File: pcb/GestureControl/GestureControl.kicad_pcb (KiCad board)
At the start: 4 copper layers, 95.3 x 95.3 mm, 179 parts, among them J1 Conn_01x04_I2I-LCD, J10 EXTERN I2C, J11 Conn_01x02, J12 Conn_01x02, J17 Conn_01x01, J18 Conn_01x01, J19 Conn_01x01, J2 BATT, J3 Conn_01x08, J4 Conn_01x06, J5 Conn_01x10, J6 Conn_01x08, J7 FTDI, J8 Conn_01x06, J9 UART, SW1 SW1, SW2 SW2, U1 AP5100_3.3, U10 VL53L3CXV0DH_RIGHT, U11 VL53L3CXV0DH_LEFT, U12 VL53L3CXV0DH_CENTER, U13 VL53L3CXV0DH_CENTER, U2 AP5100_3.3, U3 VL53L3CXV0DH_CENTER, U4 VL53L3CXV0DH_RIGHT, U5 VL53L3CXV0DH_LEFT, U6 STM32L151RETx, U7 STM32F401RETx, U8 VL53L3CXV0DH_RIGHT, U9 VL53L3CXV0DH_LEFT, Y1 8MHz, Y2 32kHz

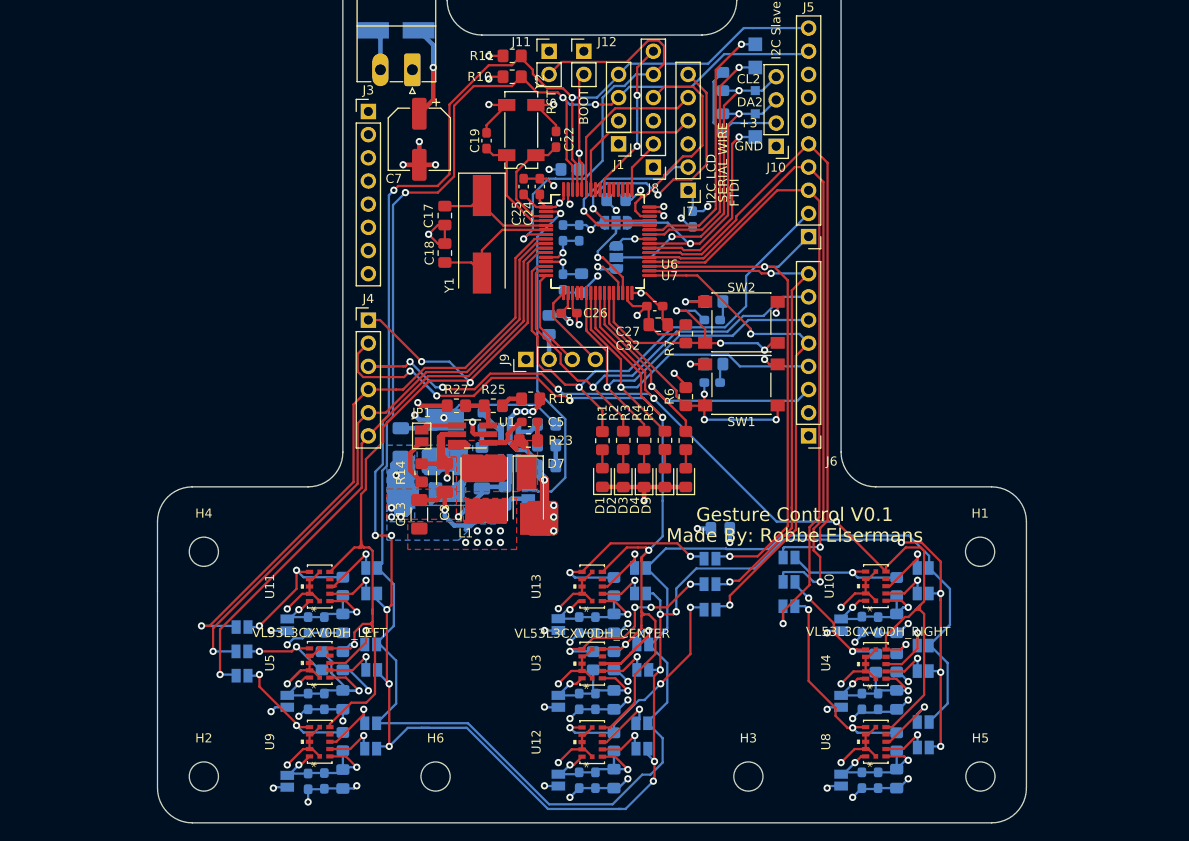
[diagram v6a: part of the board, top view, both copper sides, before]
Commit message: pcb groter maken
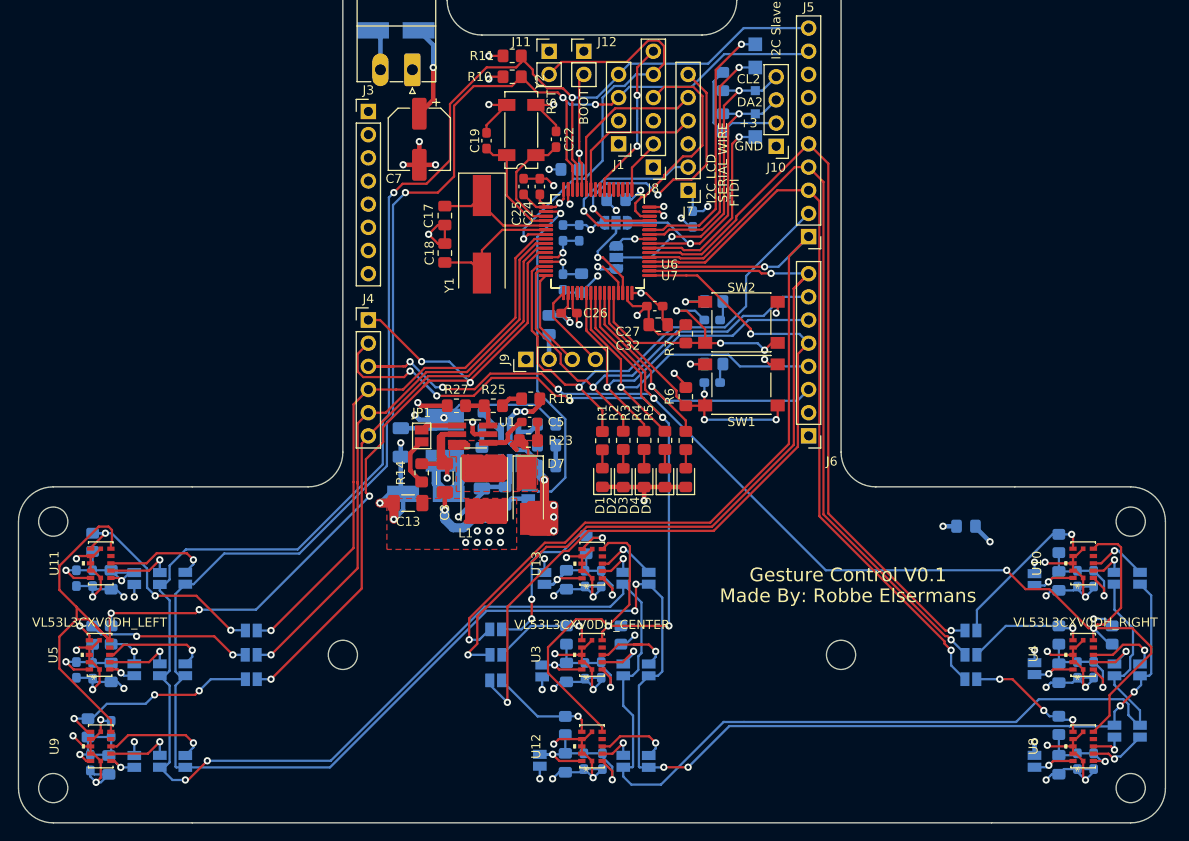
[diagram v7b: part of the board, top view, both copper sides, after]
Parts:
- moved H5 105.4 mm to (87.4, 100.1)
- moved H2 101.6 mm to (205.5, 129.3)
- moved H4 30.7 mm to (87.4, 129.3)
- moved R36 28.0 mm to (91.2, 122.7)
- moved R17 27.9 mm to (91.7, 102.3)
- moved C12 26.9 mm to (187.4, 100.6)
- moved C43 25.9 mm to (89.9, 106.3)
- moved C51 25.9 mm to (91.7, 106.3)
- moved C39 25.9 mm to (201.4, 106.3)
- moved C45 25.8 mm to (93.7, 106.4)
- moved C44 25.7 mm to (91.4, 126.5)
- moved C46 25.7 mm to (93.5, 126.7)
- moved C40 25.6 mm to (201.4, 116.3)
- moved C15 25.6 mm to (89.9, 116.3)
- moved C14 25.6 mm to (91.7, 116.4)
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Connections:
- J3 pad 1: Net-(J3-Pad1) -> (no net)
- J3 pad 2: Net-(J3-Pad2) -> (no net)
- J3 pad 3: Net-(J3-Pad3) -> (no net)
- J3 pad 8: Net-(J3-Pad8) -> (no net)
- J5 pad 6: Net-(J5-Pad6) -> (no net)
- J6 pad 1: Net-(J6-Pad1) -> (no net)
- J6 pad 2: Net-(J6-Pad2) -> (no net)
- U10 pad 8: Net-(U10-Pad8) -> (no net)
- U11 pad 8: Net-(U11-Pad8) -> (no net)
- U12 pad 8: Net-(U12-Pad8) -> (no net)
- U13 pad 8: Net-(U13-Pad8) -> (no net)
- U3 pad 8: Net-(U3-Pad8) -> (no net)
- U4 pad 8: Net-(U4-Pad8) -> (no net)
- U5 pad 8: Net-(U5-Pad8) -> (no net)
- U6 pad 20: Net-(U6-Pad20) -> (no net)
- U6 pad 21: Net-(U6-Pad21) -> (no net)
- U6 pad 50: Net-(U6-Pad50) -> (no net)
- U6 pad 51: Net-(U6-Pad51) -> (no net)
- U6 pad 52: Net-(U6-Pad52) -> (no net)
- U6 pad 53: Net-(U6-Pad53) -> (no net)
- U6 pad 54: Net-(U6-Pad54) -> (no net)
- U6 pad 56: Net-(U6-Pad56) -> (no net)
- U6 pad 57: Net-(U6-Pad57) -> (no net)
- U7 pad 20: Net-(U7-Pad20) -> (no net)
- U7 pad 21: Net-(U7-Pad21) -> (no net)
- U7 pad 50: Net-(U7-Pad50) -> (no net)
- U7 pad 51: Net-(U7-Pad51) -> (no net)
- U7 pad 52: Net-(U7-Pad52) -> (no net)
- U7 pad 53: Net-(U7-Pad53) -> (no net)
- U7 pad 54: Net-(U7-Pad54) -> (no net)
- U7 pad 56: Net-(U7-Pad56) -> (no net)
- U7 pad 57: Net-(U7-Pad57) -> (no net)
- U8 pad 8: Net-(U8-Pad8) -> (no net)
- U9 pad 8: Net-(U9-Pad8) -> (no net)
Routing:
- net SCL1: track 263.4 -> 322.2 mm, vias 16 -> 4
- net SDA1: track 249.7 -> 305.3 mm, vias 3 -> 9
- net GPIOI_0: track 98.2 -> 133.8 mm, vias 3 -> 5
- net _XSHUT_1: track 58.2 -> 90.5 mm
- net +3V3: track 517.2 -> 549.2 mm, vias 35 -> 34
- net _XSHUT_4: track 57.7 -> 89.3 mm
- net _XSHUT_7: track 54.9 -> 85.5 mm
- net /OUT5.0: track 40.4 -> 13.8 mm
- net GPIOI_2: track 124.9 -> 148.4 mm
- net XSHUT_7: track 25.5 -> 11.9 mm, vias 3 -> 1
- net _XSHUT_2: track 73.3 -> 84.5 mm
- net GPIOI_1: track 115.7 -> 126.3 mm
- net XSHUT_3: track 10.9 -> 21.5 mm, vias 2 -> 3
- net XSHUT_0: track 16.0 -> 26.2 mm, vias 2 -> 3
- net XSHUT_4: track 21.6 -> 11.5 mm, vias 4 -> 1
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- removed copper zone on B.Cu, net /OUT5.0
- removed copper zone on B.Cu, net GND
- removed copper zone on F.Cu, net GND
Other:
- board size 95.3 x 95.3 mm -> 125.7 x 95.3 mm

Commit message: add PCB V12
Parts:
- removed C43, C44, C47, C48, C49, C50, C51, C52: 100n, Capacitor_SMD:C_0603_1608Metric_Pad1.08x0.95mm_HandSolder
- removed C45, C46, C53, C54, C55: 4.7µ, Capacitor_SMD:C_0805_2012Metric_Pad1.18x1.45mm_HandSolder
- removed JP10, JP11, JP12, JP14, JP15, JP16, JP17, JP18, JP19, JP20, JP21, JP22, JP23, JP27, JP28, JP29, JP30, JP31, JP32, JP33, JP34, JP35, JP36, JP37, JP38, JP39, JP40, JP41, JP42, JP43, JP44, JP5, JP6, JP7, JP8, JP9: SolderJumper_2_Open, Jumper:SolderJumper-2_P1.3mm_Open_Pad1.0x1.5mm
- removed R33, R34, R35, R36: 10k, Resistor_SMD:R_0805_2012Metric_Pad1.20x1.40mm_HandSolder
- removed U10: VL53L3CXV0DH_RIGHT, VL53L3CX:VL53L3CXV0DH&slash_1
- removed U11, U9: VL53L3CXV0DH_LEFT, VL53L3CX:VL53L3CXV0DH&slash_1
- removed U12, U13: VL53L3CXV0DH_CENTER, VL53L3CX:VL53L3CXV0DH&slash_1
- added C20: 100n, Capacitor_SMD:C_0603_1608Metric_Pad1.08x0.95mm_HandSolder, B.Cu at (201.4, 129.6)
- added C21: 100n, Capacitor_SMD:C_0603_1608Metric_Pad1.08x0.95mm_HandSolder, B.Cu at (239.5, 129.6)
- added H10: MountingHole, MountingHole:MountingHole_3.2mm_M3, F.Cu at (111.5, 108.5)
- added H11: MountingHole, MountingHole:MountingHole_3.2mm_M3, F.Cu at (187.7, 143.4)
- added H12: MountingHole, MountingHole:MountingHole_3.2mm_M3, F.Cu at (187.7, 118.0)
- added H13: MountingHole, MountingHole:MountingHole_3.2mm_M3, F.Cu at (225.8, 118.0)
- added H14: MountingHole, MountingHole:MountingHole_3.2mm_M3, F.Cu at (225.8, 143.4)
- added H15: MountingHole, MountingHole:MountingHole_3.2mm_M3, F.Cu at (251.2, 118.0)
- added H16: MountingHole, MountingHole:MountingHole_3.2mm_M3, F.Cu at (251.2, 143.4)
- added H7: MountingHole, MountingHole:MountingHole_3.2mm_M3, F.Cu at (138.2, 108.5)
- added H8: MountingHole, MountingHole:MountingHole_3.2mm_M3, F.Cu at (111.5, 152.9)
- added H9: MountingHole, MountingHole:MountingHole_3.2mm_M3, F.Cu at (138.2, 152.9)
- added J13: 690367291076, WR-MM Female SMT Connector:WR-MM_Female_SMT_Connector, B.Cu at (162.3, 136.4)
- added J14: 690367291076, WR-MM Female SMT Connector:WR-MM_Female_SMT_Connector, B.Cu at (200.4, 136.4)
- added J15: 690367291076, WR-MM Female SMT Connector:WR-MM_Female_SMT_Connector, B.Cu at (238.5, 136.4)
- added J16: 690367291076, WR-MM Female SMT Connector:WR-MM_Female_SMT_Connector, B.Cu at (124.8, 148.7)
- added J20: 690367291076, WR-MM Female SMT Connector:WR-MM_Female_SMT_Connector, B.Cu at (124.8, 112.6)
- added J21: 690367291076, WR-MM Female SMT Connector:WR-MM_Female_SMT_Connector, B.Cu at (124.8, 137.4)
- added TP10: TestPoint, TestPoint:TestPoint_Pad_D2.0mm, B.Cu at (200.2, 115.6)
- added TP11: TestPoint, TestPoint:TestPoint_Pad_D2.0mm, B.Cu at (197.1, 118.9)
- added TP12: TestPoint, TestPoint:TestPoint_Pad_D2.0mm, B.Cu at (200.2, 118.9)
- added TP13: TestPoint, TestPoint:TestPoint_Pad_D2.0mm, B.Cu at (203.2, 115.6)
- added TP14: TestPoint, TestPoint:TestPoint_Pad_D2.0mm, B.Cu at (203.2, 118.9)
- added TP15: TestPoint, TestPoint:TestPoint_Pad_D2.0mm, B.Cu at (235.2, 115.6)
- added TP16: TestPoint, TestPoint:TestPoint_Pad_D2.0mm, B.Cu at (238.3, 115.6)
- added TP17: TestPoint, TestPoint:TestPoint_Pad_D2.0mm, B.Cu at (235.2, 118.9)
- added TP18: TestPoint, TestPoint:TestPoint_Pad_D2.0mm, B.Cu at (238.3, 118.9)
- added TP19: TestPoint, TestPoint:TestPoint_Pad_D2.0mm, B.Cu at (241.3, 115.6)
- added TP20: TestPoint, TestPoint:TestPoint_Pad_D2.0mm, B.Cu at (241.3, 118.9)
- added TP3: TestPoint, TestPoint:TestPoint_Pad_D2.0mm, B.Cu at (158.9, 115.6)
- added TP4: TestPoint, TestPoint:TestPoint_Pad_D2.0mm, B.Cu at (162.1, 115.6)
- added TP5: TestPoint, TestPoint:TestPoint_Pad_D2.0mm, B.Cu at (158.9, 118.9)
- added TP6: TestPoint, TestPoint:TestPoint_Pad_D2.0mm, B.Cu at (162.1, 118.9)
- added TP7: TestPoint, TestPoint:TestPoint_Pad_D2.0mm, B.Cu at (165.2, 115.6)
- added TP8: TestPoint, TestPoint:TestPoint_Pad_D2.0mm, B.Cu at (165.2, 118.9)
- added TP9: TestPoint, TestPoint:TestPoint_Pad_D2.0mm, B.Cu at (197.1, 115.6)
- C16: value 4.7µ -> 100n; footprint Capacitor_SMD:C_0805_2012Metric_Pad1.18x1.45mm_HandSolder -> Capacitor_SMD:C_0603_1608Metric_Pad1.08x0.95mm_HandSolder
- C36: value 100n -> 4.7µ; footprint Capacitor_SMD:C_0603_1608Metric_Pad1.08x0.95mm_HandSolder -> Capacitor_SMD:C_0805_2012Metric_Pad1.18x1.45mm_HandSolder
- C39, C40, C41, C42: value 100n -> 10µ; footprint Capacitor_SMD:C_0603_1608Metric_Pad1.08x0.95mm_HandSolder -> Capacitor_SMD:C_1206_3216Metric_Pad1.33x1.80mm_HandSolder
- U3: value VL53L3CXV0DH_CENTER -> VL53L3CXV0DH_1
- U4, U8: value VL53L3CXV0DH_RIGHT -> VL53L3CXV0DH_1
- U5: value VL53L3CXV0DH_LEFT -> VL53L3CXV0DH_1
- moved R17 149.7 mm to (235.7, 143.3)
- moved C15 148.4 mm to (237.7, 129.6), turned to 90 degrees
- moved J19 130.3 mm to (51.4, 112.8), turned to 270 degrees
- moved D6 129.8 mm to (49.9, 152.2), turned to 270 degrees
- moved H5 127.0 mm to (213.1, 118.0)
- moved J18 126.8 mm to (54.0, 112.8), turned to 270 degrees
- moved J12 124.9 mm to (52.2, 131.6), turned to 90 degrees
- moved J11 124.8 mm to (52.2, 135.4), turned to 90 degrees
- moved R11 124.1 mm to (52.7, 139.4), turned to 90 degrees
- moved R22 123.5 mm to (55.5, 116.3), turned to 0 degrees
- moved J2 123.4 mm to (54.2, 150.4), turned to 270 degrees
- moved TP2 123.4 mm to (56.5, 112.8), turned to 270 degrees
- moved R10 120.8 mm to (55.0, 139.4), turned to 90 degrees
- moved TP1 119.9 mm to (59.1, 112.8), turned to 270 degrees
- moved J3 118.3 mm to (58.8, 155.2), turned to 90 degrees
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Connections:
- C10 pad 1: /VL53L3CX center/PWR1 -> +3V3
- C14 pad 1: /VL53L3CX left/PWR1 -> +3V3
- C15 pad 1: /VL53L3CX left/PWR1 -> +3V3
- C16 pad 1: /VL53L3CX left/PWR1 -> +3V3
- C35 pad 1: /VL53L3CX center/PWR0 -> +3V3
- C36 pad 1: /VL53L3CX center/PWR2 -> +3V3
- C37 pad 1: /VL53L3CX center/PWR0 -> +3V3
- C38 pad 1: /VL53L3CX center/PWR2 -> +3V3
- C39 pad 1: /VL53L3CX right/PWR0 -> +3V3
- C40 pad 1: /VL53L3CX right/PWR1 -> +3V3
- C41 pad 1: /VL53L3CX right/PWR2 -> +3V3
- C42 pad 1: /VL53L3CX right/PWR0 -> +3V3
- C8 pad 1: /VL53L3CX center/PWR1 -> +3V3
- C9 pad 1: /VL53L3CX center/PWR1 -> +3V3
- J4 pad 1: GPIOI_0 -> XSHUT_0
- J4 pad 2: GPIOI_1 -> XSHUT_1
- J4 pad 3: GPIOI_2 -> XSHUT_2
- J4 pad 4: _XSHUT_0 -> XSHUT_3
- J4 pad 5: _XSHUT_3 -> SW_1
- J4 pad 6: _XSHUT_6 -> SW_2
- J5 pad 1: _XSHUT_1 -> (no net)
- J5 pad 2: LED_1 -> (no net)
- J5 pad 3: _XSHUT_8 -> GPIOI_0
- J5 pad 4: _XSHUT_5 -> GPIOI_1
- J5 pad 5: _XSHUT_2 -> GPIOI_2
- J5 pad 6: (no net) -> GPIOI_3
- J6 pad 5: _XSHUT_7 -> LED_3
- J6 pad 6: LED_3 -> LED_2
- J6 pad 7: LED_2 -> LED_1
- J6 pad 8: _XSHUT_4 -> (no net)
- R13 pad 1: /VL53L3CX center/PWR0 -> +3V3
- R13 pad 2: XSHUT_1 -> GPIOI_2
- R16 pad 2: GPIOI_0 -> XSHUT_2
- R17 pad 1: /VL53L3CX left/PWR0 -> +3V3
- R17 pad 2: XSHUT_0 -> GPIOI_3
- R29 pad 1: /VL53L3CX center/PWR1 -> +3V3
- R29 pad 2: XSHUT_4 -> XSHUT_1
- R30 pad 1: /VL53L3CX center/PWR2 -> +3V3
- R30 pad 2: XSHUT_7 -> XSHUT_3
- R31 pad 2: GPIOI_2 -> GPIOI_0
- R32 pad 1: /VL53L3CX right/PWR0 -> +3V3
- R32 pad 2: XSHUT_2 -> XSHUT_0
- U3 pad 1: /VL53L3CX center/PWR1 -> +3V3
- U3 pad 10: Net-(JP20-Pad1) -> SCL1
- U3 pad 11: /VL53L3CX center/PWR1 -> +3V3
- U3 pad 5: XSHUT_4 -> XSHUT_0
- U3 pad 7: GPIOI_1 -> GPIOI_0
- U3 pad 9: Net-(JP21-Pad1) -> SDA1
- U4 pad 1: /VL53L3CX right/PWR1 -> +3V3
- U4 pad 10: Net-(JP32-Pad1) -> SCL1
- U4 pad 11: /VL53L3CX right/PWR1 -> +3V3
- U4 pad 5: XSHUT_5 -> XSHUT_1
- U4 pad 7: GPIOI_2 -> GPIOI_1
- U4 pad 9: Net-(JP33-Pad1) -> SDA1
- U5 pad 1: /VL53L3CX left/PWR1 -> +3V3
- U5 pad 10: Net-(JP41-Pad1) -> SCL1
- U5 pad 11: /VL53L3CX left/PWR1 -> +3V3
- U5 pad 5: XSHUT_3 -> XSHUT_2
- U5 pad 7: GPIOI_0 -> GPIOI_2
- U5 pad 9: Net-(JP42-Pad1) -> SDA1
- U6 pad 10: _XSHUT_6 -> XSHUT_2
- U6 pad 11: GPIOI_0 -> XSHUT_3
- U6 pad 24: GPIOI_1 -> (no net)
- U6 pad 25: GPIOI_2 -> (no net)
- U6 pad 33: _XSHUT_7 -> GPIOI_0
- U6 pad 34: _XSHUT_4 -> GPIOI_1
- U6 pad 35: _XSHUT_1 -> GPIOI_2
- U6 pad 36: _XSHUT_8 -> GPIOI_3
- U6 pad 37: _XSHUT_5 -> (no net)
- U6 pad 38: _XSHUT_2 -> (no net)
- U6 pad 8: _XSHUT_0 -> XSHUT_0
- U6 pad 9: _XSHUT_3 -> XSHUT_1
- U7 pad 10: _XSHUT_6 -> XSHUT_2
- U7 pad 11: GPIOI_0 -> XSHUT_3
- U7 pad 24: GPIOI_1 -> (no net)
- U7 pad 25: GPIOI_2 -> (no net)
- U7 pad 33: _XSHUT_7 -> GPIOI_0
- U7 pad 34: _XSHUT_4 -> GPIOI_1
- U7 pad 35: _XSHUT_1 -> GPIOI_2
- U7 pad 36: _XSHUT_8 -> GPIOI_3
- U7 pad 37: _XSHUT_5 -> (no net)
- U7 pad 38: _XSHUT_2 -> (no net)
- U7 pad 8: _XSHUT_0 -> XSHUT_0
- U7 pad 9: _XSHUT_3 -> XSHUT_1
- U8 pad 1: /VL53L3CX right/PWR2 -> +3V3
- U8 pad 10: Net-(JP34-Pad1) -> SCL1
- U8 pad 11: /VL53L3CX right/PWR2 -> +3V3
- U8 pad 5: XSHUT_8 -> XSHUT_3
- U8 pad 7: GPIOI_2 -> GPIOI_3
- U8 pad 9: Net-(JP35-Pad1) -> SDA1
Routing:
- net GPIOI_3: track 0.00 -> 243.2 mm, vias 0 -> 4
- net XSHUT_3: track 21.5 -> 255.7 mm, vias 3 -> 5
- net XSHUT_2: track 17.7 -> 241.2 mm, vias 1 -> 9
- net XSHUT_0: track 26.2 -> 198.5 mm
- net +3V3: track 549.2 -> 700.3 mm, vias 34 -> 48
- net SDA1: track 305.3 -> 455.6 mm, vias 9 -> 14
- net XSHUT_1: track 21.8 -> 170.5 mm, vias 3 -> 7
- net SCL1: track 322.2 -> 440.3 mm, vias 4 -> 17
- net _XSHUT_1: track 90.5 -> 0.00 mm, vias 2 -> 0
- net _XSHUT_4: track 89.3 -> 0.00 mm, vias 2 -> 0
- net SW_2: track 31.7 -> 117.3 mm, vias 3 -> 7
- net _XSHUT_7: track 85.5 -> 0.00 mm, vias 2 -> 0
- net _XSHUT_2: track 84.5 -> 0.00 mm, vias 1 -> 0
- net SW_1: track 31.9 -> 115.2 mm, vias 3 -> 7
- net _XSHUT_5: track 82.4 -> 0.00 mm, vias 1 -> 0
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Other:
- board size 125.7 x 95.3 mm -> 214.8 x 54.6 mm
- board text added: "GND 3V3"
- board text added: "SCL XSHUT"
- board text added: "SDA GPIOI"
- board text removed: "Gesture Control V0.1"
- board text removed: "Made By: Robbe Elsermans"
